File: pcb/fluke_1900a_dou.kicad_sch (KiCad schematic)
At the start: 71 parts, among them J3 DOU CONNECTOR, P3 USB_B, Q1 Si2336DS, Q2 Si2336DS, Q3 Si2336DS, Q4 Si2336DS, U1 TPS71533, U2 MSP430G2452IN20, U3 SFH617A-4, U4 SFH617A-4, U5 SFH617A-4, U6 CH340N, X1 DEBUG

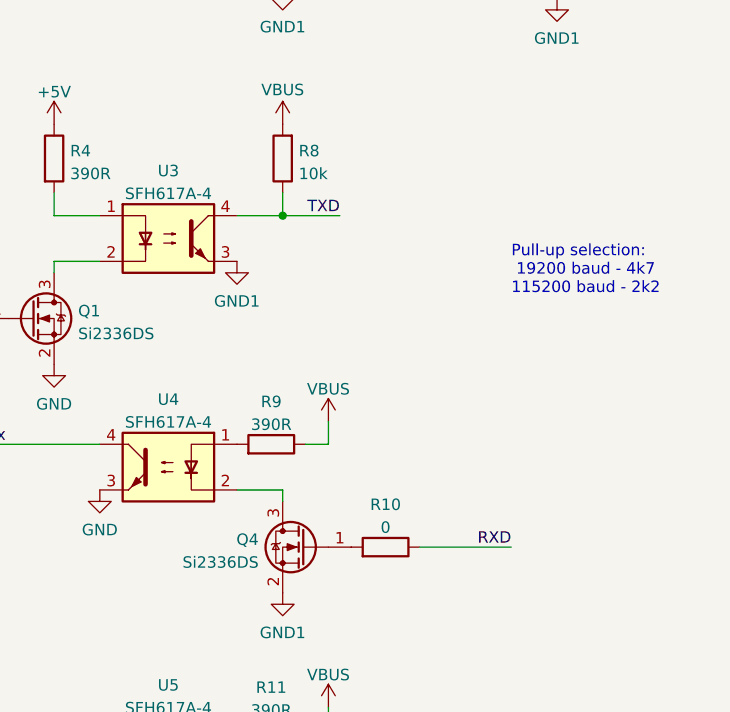
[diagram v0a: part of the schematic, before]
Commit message: Tx must be connected to RXD on the CH340N
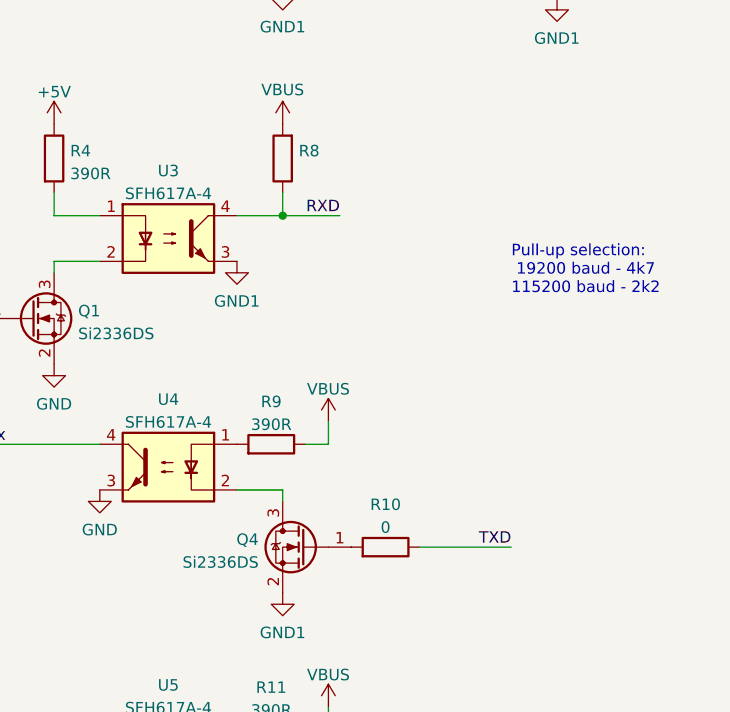
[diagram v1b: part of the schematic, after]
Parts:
- R8: value 10k -> (none)
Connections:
- net RXD: now also R8.1, U3.4; no longer R10.1
- net TXD: now also R10.1; no longer R8.1, U3.4
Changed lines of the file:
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@@
     (effects (font (size 1.27 1.27)) (justify right bottom))
   )
-  (label "TXD" (at 234.95 80.01 180)
+  (label "RXD" (at 234.95 80.01 180)
     (effects (font (size 1.27 1.27)) (justify right bottom))
   )
@@
     (effects (font (size 1.27 1.27)) (justify left bottom))
   )
-  (label "RXD" (at 254 116.84 180)
+  (label "TXD" (at 254 116.84 180)
     (effects (font (size 1.27 1.27)) (justify right bottom))
   )
@@
       (effects (font (size 1.27 1.27)) (justify right))
     )
-    (property "Value" "10k" (id 1) (at 230.378 75.3622 0)
+    (property "Value" "" (id 1) (at 230.378 75.3622 0)
       (effects (font (size 1.27 1.27)) (justify right))
     )
@@
     )
     (path "/cd94d6cd-612d-423f-a515-005a8c5d535b"
-      (reference "R8") (unit 1) (value "10k") (footprint "Resistor_SMD:R_0805_2012Metric")
+      (reference "R8") (unit 1) (value "4k7") (footprint "Resistor_SMD:R_0805_2012Metric")
     )
     (path "/ca4812d8-2794-4cc5-9279-9a80c741be33"

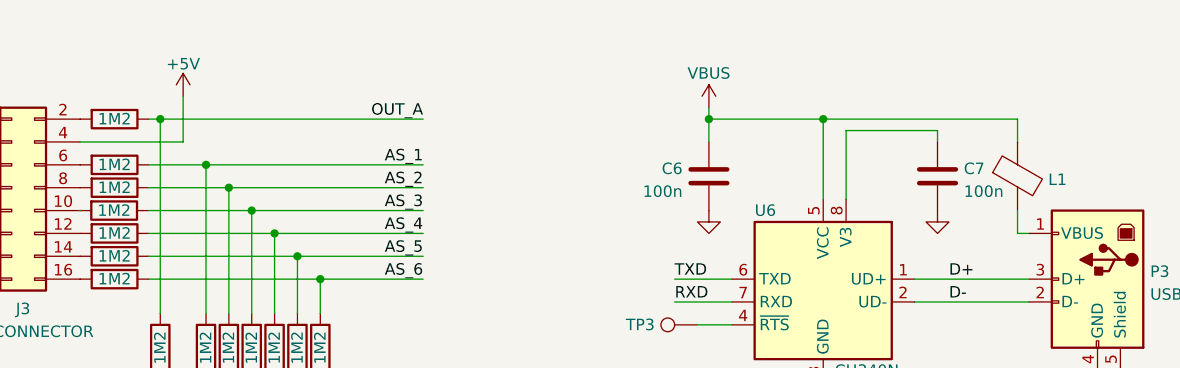
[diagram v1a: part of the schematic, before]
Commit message: add fuses F1, F2 to protect device and USB host
In case in anything ever does go wrong, the fuse should protect the
device from any harm. The same makes sense for the USB side of things.
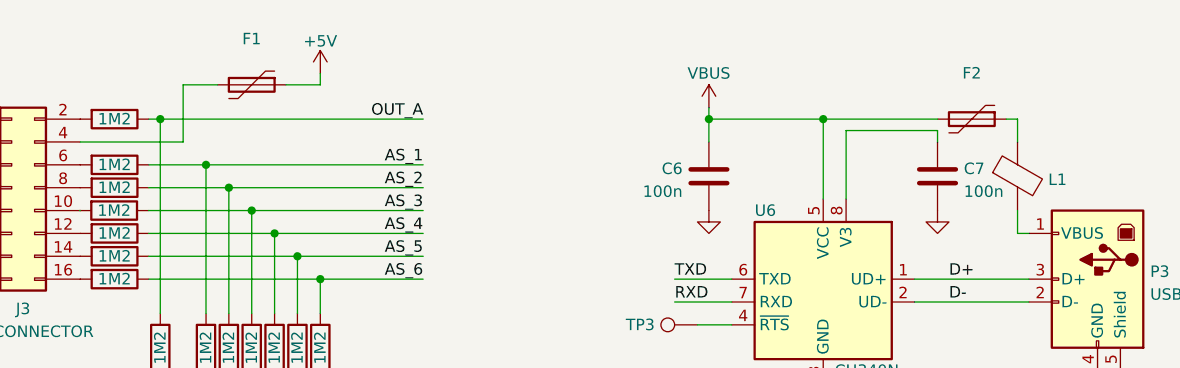
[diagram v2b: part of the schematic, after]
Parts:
- added F1, F2: (no value), symbol Device:Polyfuse
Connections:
- net +5V: now also F1.1; no longer J3.4 (Pin_4)
- net VBUS: now also F2.2; no longer L1.1
- new net: F2.1, L1.1
- new net: F1.2, J3.4 (Pin_4)
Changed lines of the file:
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@@
     (stroke (width 0) (type default) (color 0 0 0 0))
   )
-  (wire (pts (xy 157.48 22.86) (xy 157.48 27.94))
+  (wire (pts (xy 157.48 21.59) (xy 157.48 27.94))
     (stroke (width 0) (type default) (color 0 0 0 0))
   )
@@
     (stroke (width 0) (type default) (color 0 0 0 0))
   )
+  (wire (pts (xy 168.91 21.59) (xy 172.72 21.59))
+    (stroke (width 0) (type default) (color 0 0 0 0))
+  )
   (wire (pts (xy 167.64 38.1) (xy 167.64 46.99))
     (stroke (width 0) (type default) (color 0 0 0 0))
@@
     (stroke (width 0) (type default) (color 0 0 0 0))
   )
+  (wire (pts (xy 241.3 25.4) (xy 228.6 25.4))
+    (stroke (width 0) (type default) (color 0 0 0 0))
+  )
   (wire (pts (xy 170.18 54.61) (xy 170.18 55.88))
     (stroke (width 0) (type default) (color 0 0 0 0))
@@
     (stroke (width 0) (type default) (color 0 0 0 0))
   )
+  (wire (pts (xy 161.29 21.59) (xy 157.48 21.59))
+    (stroke (width 0) (type default) (color 0 0 0 0))
+  )
   (wire (pts (xy 165.1 110.49) (xy 177.8 110.49))
     (stroke (width 0) (type default) (color 0 0 0 0))
@@
     (stroke (width 0) (type default) (color 0 0 0 0))
   )
-  (wire (pts (xy 250.19 25.4) (xy 228.6 25.4))
+  (wire (pts (xy 250.19 25.4) (xy 248.92 25.4))
     (stroke (width 0) (type default) (color 0 0 0 0))
   )
@@
   )
   (wire (pts (xy 116.84 55.88) (xy 114.3 55.88))
+    (stroke (width 0) (type default) (color 0 0 0 0))
+  )
+  (wire (pts (xy 172.72 21.59) (xy 172.72 20.32))
     (stroke (width 0) (type default) (color 0 0 0 0))
   )
@@
     (pin "2")
   )
+  (symbol (lib_id "Device:Polyfuse") (at 245.11 25.4 270) (unit 1)
+    (in_bom yes) (on_board yes) (fields_autoplaced)
+    (property "Reference" "F2" (id 0) (at 245.11 20.3032 90))
+    (property "Value" "" (id 1) (at 245.11 22.8401 90))
+    (property "Footprint" "" (id 2) (at 240.03 26.67 0)
+      (effects (font (size 1.27 1.27)) (justify left) hide)
+    )
+    (property "Datasheet" "~" (id 3) (at 245.11 25.4 0)
+      (effects (font (size 1.27 1.27)) hide)
+    )
+    (property "MPN" "FSMD010-0805-R" (id 4) (at 245.11 25.4 90)
+      (effects (font (size 1.27 1.27)) hide)
+    )
+    (pin "1")
+    (pin "2")
+  )
   (symbol (lib_id "Device:R") (at 111.76 50.8 0) (unit 1)
     (in_bom yes) (on_board yes)
@@
     )
     (pin "1")
+  )
+  (symbol (lib_id "Device:Polyfuse") (at 165.1 21.59 270) (unit 1)
+    (in_bom yes) (on_board yes) (fields_autoplaced)
+    (property "Reference" "F1" (id 0) (at 165.1 16.4932 90))
+    (property "Value" "" (id 1) (at 165.1 19.0301 90))
+    (property "Footprint" "" (id 2) (at 160.02 22.86 0)
+      (effects (font (size 1.27 1.27)) (justify left) hide)
+    )
+    (property "Datasheet" "~" (id 3) (at 165.1 21.59 0)
+      (effects (font (size 1.27 1.27)) hide)
+    )
+    (property "MPN" "FSMD010-0805-R" (id 4) (at 165.1 21.59 90)
+      (effects (font (size 1.27 1.27)) hide)
+    )
+    (pin "1")
+    (pin "2")
   )
   (symbol (lib_id "Device:R") (at 168.91 96.52 90) (unit 1)
@@
     (pin "9")
   )
-  (symbol (lib_id "power:+5V") (at 157.48 22.86 0) (unit 1)
-    (in_bom yes) (on_board yes)
-    (property "Reference" "#PWR0109" (id 0) (at 157.48 26.67 0)
-      (effects (font (size 1.27 1.27)) hide)
-    )
-    (property "Value" "+5V" (id 1) (at 157.48 19.2842 0))
-    (property "Footprint" "" (id 2) (at 157.48 22.86 0)
-      (effects (font (size 1.27 1.27)) hide)
-    )
-    (property "Datasheet" "" (id 3) (at 157.48 22.86 0)
+  (symbol (lib_id "power:+5V") (at 172.72 20.32 0) (unit 1)
+    (in_bom yes) (on_board yes)
+    (property "Reference" "#PWR0109" (id 0) (at 172.72 24.13 0)
+      (effects (font (size 1.27 1.27)) hide)
+    )
+    (property "Value" "+5V" (id 1) (at 172.72 16.7442 0))
+    (property "Footprint" "" (id 2) (at 172.72 20.32 0)
+      (effects (font (size 1.27 1.27)) hide)
+    )
+    (property "Datasheet" "" (id 3) (at 172.72 20.32 0)
       (effects (font (size 1.27 1.27)) hide)
     )
@@
       (reference "C7") (unit 1) (value "100n") (footprint "Capacitor_SMD:C_0805_2012Metric")
     )
+    (path "/3ead0b98-6b7d-496b-a1be-677dfd788c22"
+      (reference "F1") (unit 1) (value "100mA 0805") (footprint "Fuse:Fuse_0805_2012Metric")
+    )
+    (path "/34b1eaa7-407c-426f-9832-69cd30a56490"
+      (reference "F2") (unit 1) (value "100mA 0805") (footprint "Fuse:Fuse_0805_2012Metric")
+    )
     (path "/1d9cdadc-9036-4a95-b6db-fa7b3b74c869"

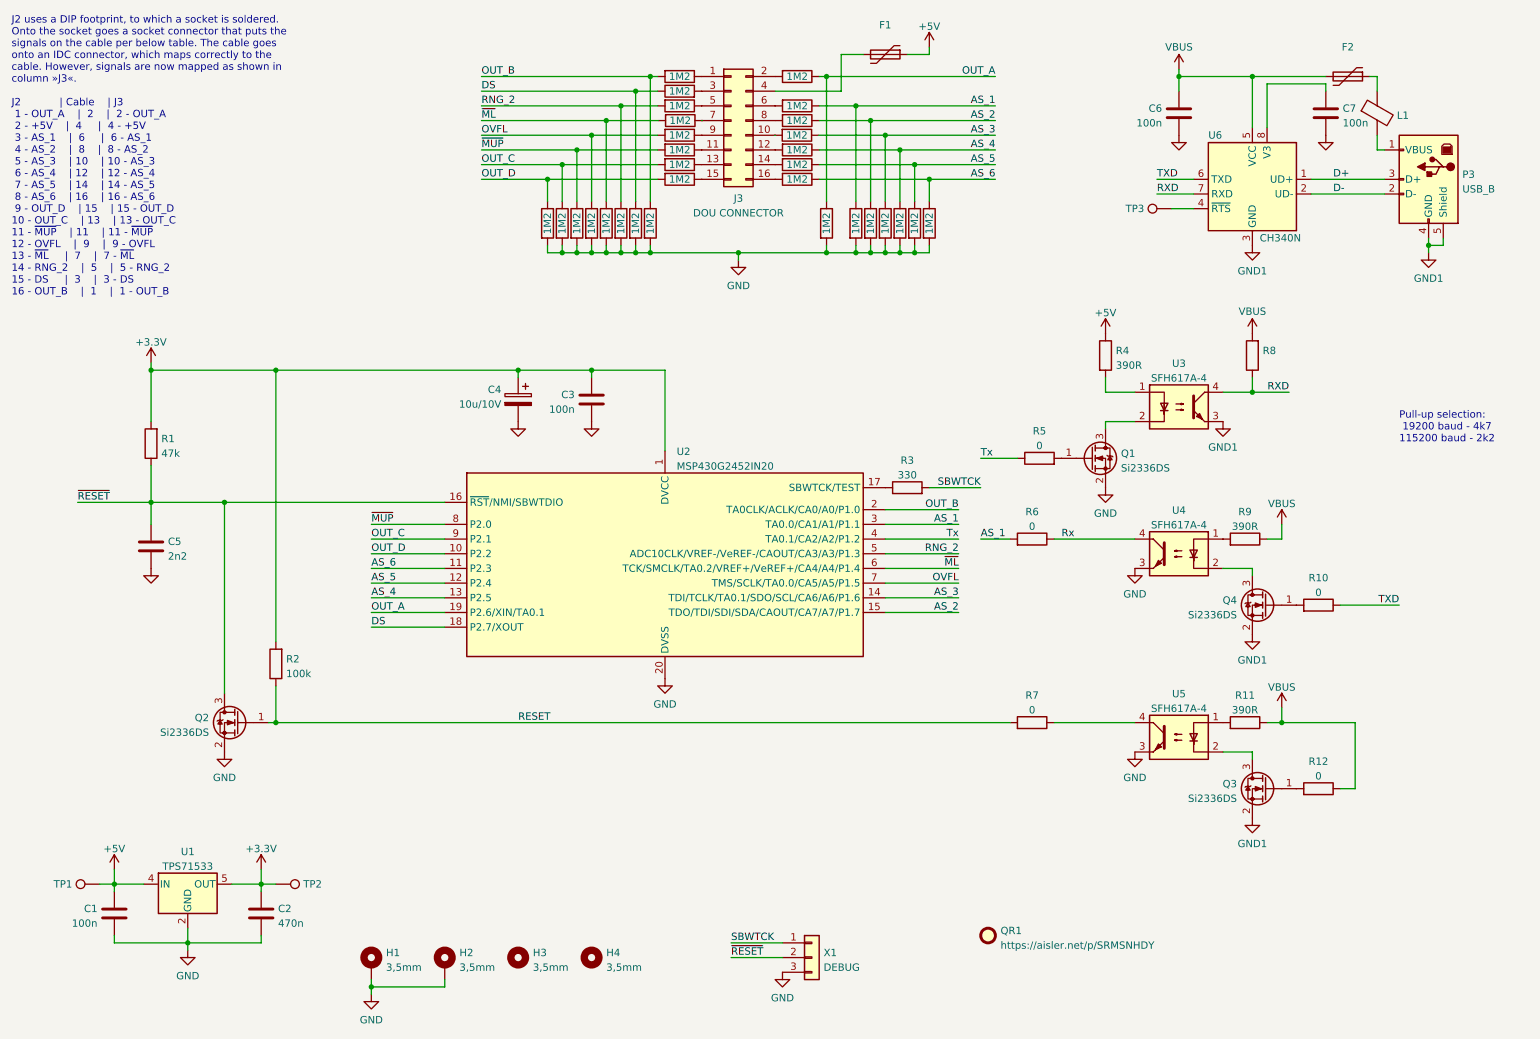
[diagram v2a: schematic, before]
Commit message: add pull-up R13 to Rx line
While the Rx line is currently not usable, it should be able to operate
at the same bitrate as the Tx line. That requires the ability to select
the pull-up accordingly.
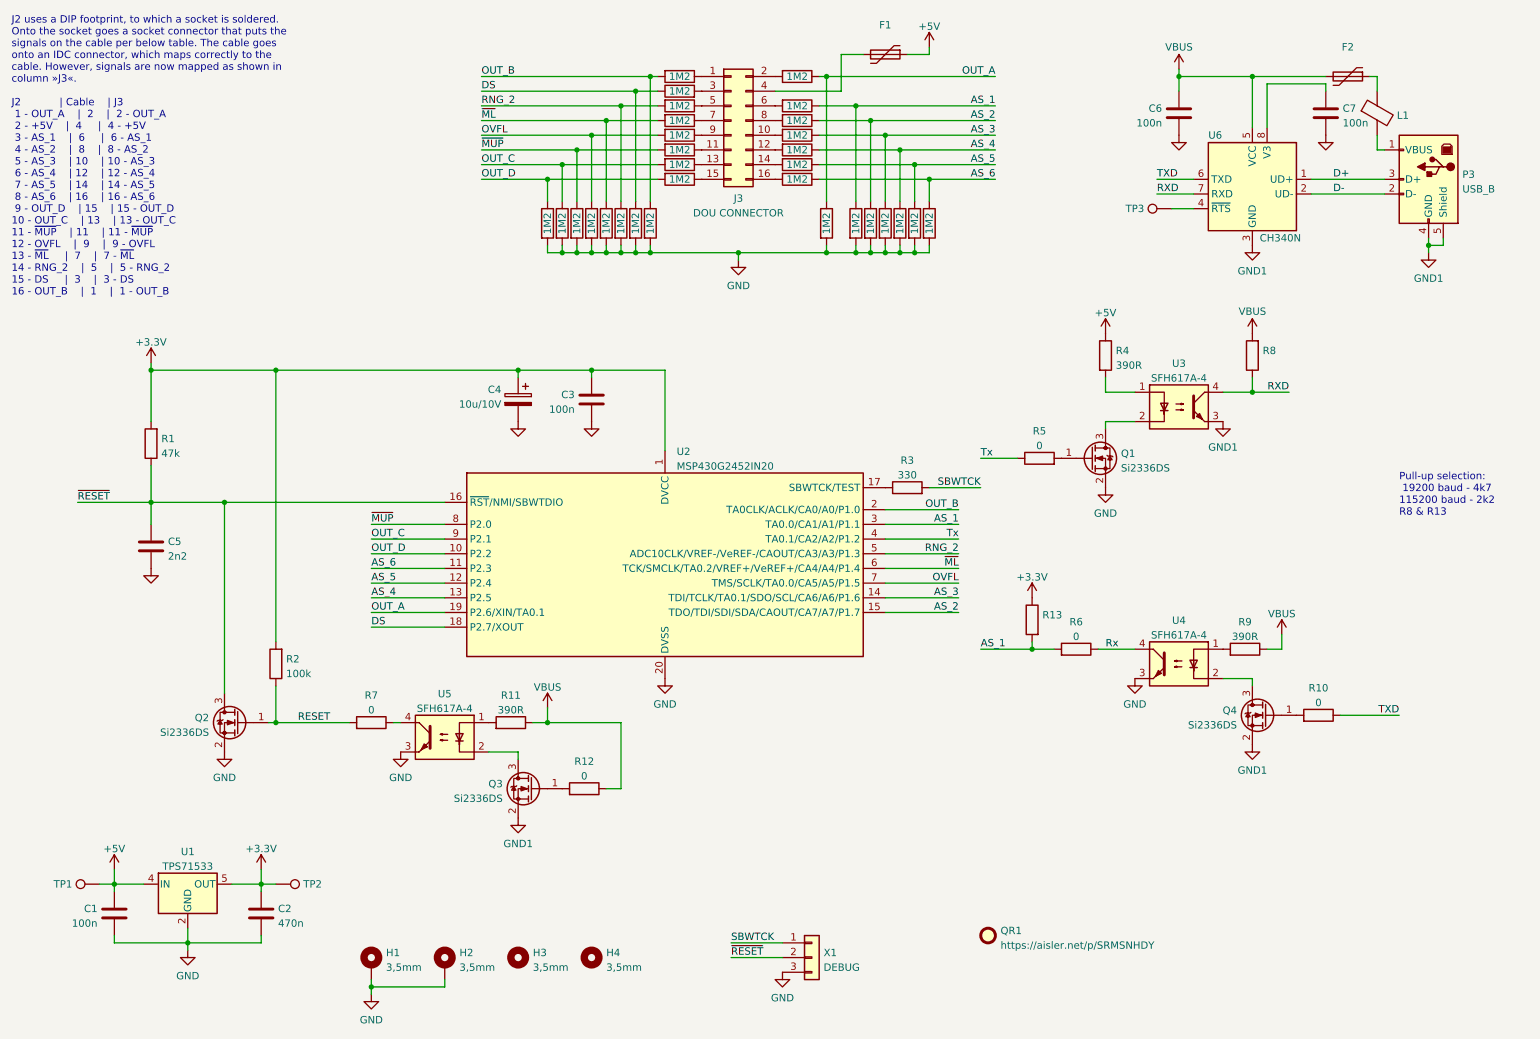
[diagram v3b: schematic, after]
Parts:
- added R13: (no value), symbol Device:R
- R20: renamed from R21; value 1.2M 0805 -> (none); footprint Resistor_SMD:R_0805_2012Metric -> (none)
- R21: renamed from R22; value 1.2M 0805 -> (none); footprint Resistor_SMD:R_0805_2012Metric -> (none)
- R22: renamed from R23; value 1.2M 0805 -> (none); footprint Resistor_SMD:R_0805_2012Metric -> (none)
- R24, R25: value 1.2M 0805 -> (none); footprint Resistor_SMD:R_0805_2012Metric -> (none)
- R28: renamed from R13; value 1.2M 0805 -> (none); footprint Resistor_SMD:R_0805_2012Metric -> (none)
- R29: renamed from R14; value 1.2M 0805 -> (none); footprint Resistor_SMD:R_0805_2012Metric -> (none)
- R30: renamed from R15; value 1.2M 0805 -> (none); footprint Resistor_SMD:R_0805_2012Metric -> (none)
- R31: renamed from R16; value 1.2M 0805 -> (none); footprint Resistor_SMD:R_0805_2012Metric -> (none)
- R32: renamed from R17; value 1.2M 0805 -> (none); footprint Resistor_SMD:R_0805_2012Metric -> (none)
- R33: renamed from R18; value 1.2M 0805 -> (none); footprint Resistor_SMD:R_0805_2012Metric -> (none)
- R34: renamed from R19; value 1.2M 0805 -> (none); footprint Resistor_SMD:R_0805_2012Metric -> (none)
- R35: renamed from R20; value 1.2M 0805 -> (none); footprint Resistor_SMD:R_0805_2012Metric -> (none)
- R36: renamed from R41; value 1.2M 0805 -> (none); footprint Resistor_SMD:R_0805_2012Metric -> (none)
- R37: renamed from R42; value 1.2M 0805 -> (none); footprint Resistor_SMD:R_0805_2012Metric -> (none)
- R38: renamed from R28; value 1.2M 0805 -> (none); footprint Resistor_SMD:R_0805_2012Metric -> (none)
- R39: renamed from R29; value 1.2M 0805 -> (none); footprint Resistor_SMD:R_0805_2012Metric -> (none)
- R40: renamed from R30; value 1.2M 0805 -> (none); footprint Resistor_SMD:R_0805_2012Metric -> (none)
- R41: renamed from R31; value 1.2M 0805 -> (none); footprint Resistor_SMD:R_0805_2012Metric -> (none)
- R42: renamed from R34; value 1.2M 0805 -> (none); footprint Resistor_SMD:R_0805_2012Metric -> (none)
- R43: renamed from R32; value 1.2M 0805 -> (none); footprint Resistor_SMD:R_0805_2012Metric -> (none)
- R44: renamed from R33; value 1.2M 0805 -> (none); footprint Resistor_SMD:R_0805_2012Metric -> (none)
- R45: renamed from R35; value 1.2M 0805 -> (none); footprint Resistor_SMD:R_0805_2012Metric -> (none)
- R46: renamed from R36; value 1.2M 0805 -> (none); footprint Resistor_SMD:R_0805_2012Metric -> (none)
- R47: renamed from R37; value 1.2M 0805 -> (none); footprint Resistor_SMD:R_0805_2012Metric -> (none)
- R48: renamed from R38; value 1.2M 0805 -> (none); footprint Resistor_SMD:R_0805_2012Metric -> (none)
- R49: renamed from R39; value 1.2M 0805 -> (none); footprint Resistor_SMD:R_0805_2012Metric -> (none)
- R50: renamed from R40; value 1.2M 0805 -> (none); footprint Resistor_SMD:R_0805_2012Metric -> (none)
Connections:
- net +3V3: now also R13.1
- net AS_1: now also R13.2
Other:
- note added: "Pull-up selection: 19200 baud - 4k7 115200 baud - 2k2 R8 & R13"
- note removed: "Pull-up selection: 19200 baud - 4k7 115200 baud - 2k2"
- moved on the sheet: Q3, Q4, R10, R11, R12, R6, R7, R9, U4, U5

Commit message: add documentation for title block and various components
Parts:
- F1, F2: value (none) -> 100mA 0805; footprint (none) -> Fuse:Fuse_0805_2012Metric
- R11, R4, R9: value (none) -> 390R 0805; footprint (none) -> Resistor_SMD:R_0805_2012Metric
- R13: value (none) -> DNP; footprint (none) -> Resistor_SMD:R_0805_2012Metric
- R20, R21, R22, R24, R25, R28, R29, R30, R31, R32, R33, R34, R35, R36, R37, R38, R39, R40, R41, R42, R43, R44, R45, R46, R47, R48, R49, R50: value (none) -> 1.2M 0805; footprint (none) -> Resistor_SMD:R_0805_2012Metric
- R8: value (none) -> 4k7
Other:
- company: (none) -> D. Kellermann
- title: (none) -> FLUKE 1900A DATA OUTPUT UNIT +USB
